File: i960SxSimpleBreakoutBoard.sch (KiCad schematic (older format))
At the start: 31 parts, among them J1 Conn_01x23, J2 Address LInes, J3 Data Lines, U1 80960Sx, U2 74HC573, U3 74HC573, U4 74HC245, U5 74HC245

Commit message: Fix a typo
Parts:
- J2: value Address LInes -> Address Lines
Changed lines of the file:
@@
 P 12450 5750
 F 0 "J2" H 12530 5742 50  0000 L CNN
-F 1 "Address LInes" H 12530 5651 50  0000 L CNN
+F 1 "Address Lines" H 12530 5651 50  0000 L CNN
 F 2 "" H 12450 5750 50  0001 C CNN
 F 3 "~" H 12450 5750 50  0001 C CNN

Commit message: Finish part selection
We shall see if the board gets too large from this change or not
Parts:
- J1: footprint (none) -> Connector_PinHeader_2.54mm:PinHeader_1x23_P2.54mm_Vertical
- J2: footprint (none) -> Connector_PinHeader_2.54mm:PinHeader_1x32_P2.54mm_Vertical
- J3: footprint (none) -> Connector_PinHeader_2.54mm:PinHeader_1x16_P2.54mm_Vertical
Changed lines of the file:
@@
 F 0 "J1" H 12530 2092 50  0000 L CNN
 F 1 "Conn_01x23" H 12530 2001 50  0000 L CNN
-F 2 "" H 12450 2050 50  0001 C CNN
+F 2 "Connector_PinHeader_2.54mm:PinHeader_1x23_P2.54mm_Vertical" H 12450 2050 50  0001 C CNN
 F 3 "~" H 12450 2050 50  0001 C CNN
 	1    12450 2050
@@
 F 0 "J2" H 12530 5742 50  0000 L CNN
 F 1 "Address Lines" H 12530 5651 50  0000 L CNN
-F 2 "" H 12450 5750 50  0001 C CNN
+F 2 "Connector_PinHeader_2.54mm:PinHeader_1x32_P2.54mm_Vertical" H 12450 5750 50  0001 C CNN
 F 3 "~" H 12450 5750 50  0001 C CNN
 	1    12450 5750
@@
 F 0 "J3" H 16630 5242 50  0000 L CNN
 F 1 "Data Lines" H 16630 5151 50  0000 L CNN
-F 2 "" H 16550 5250 50  0001 C CNN
+F 2 "Connector_PinHeader_2.54mm:PinHeader_1x16_P2.54mm_Vertical" H 16550 5250 50  0001 C CNN
 F 3 "~" H 16550 5250 50  0001 C CNN
 	1    16550 5250

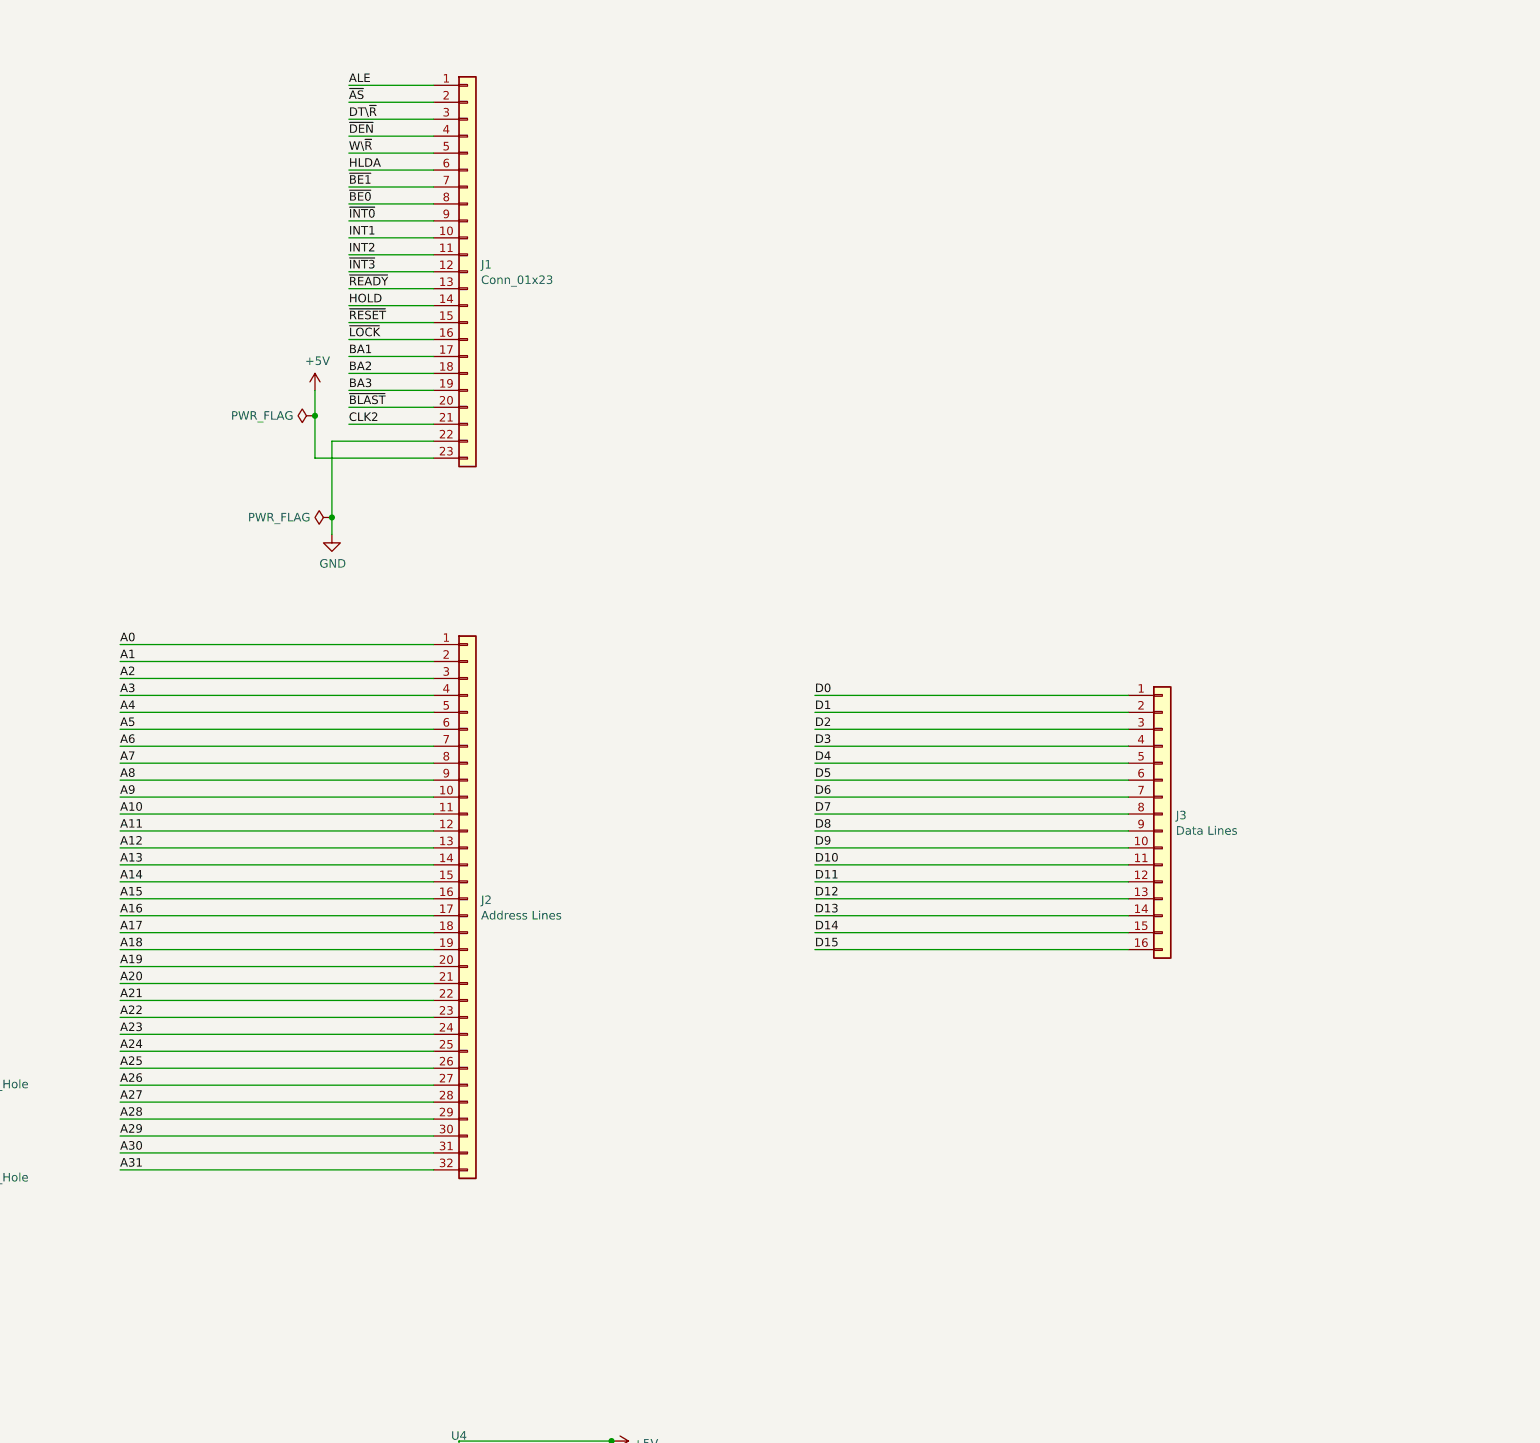
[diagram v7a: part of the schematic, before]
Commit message: Condense the pin headers further
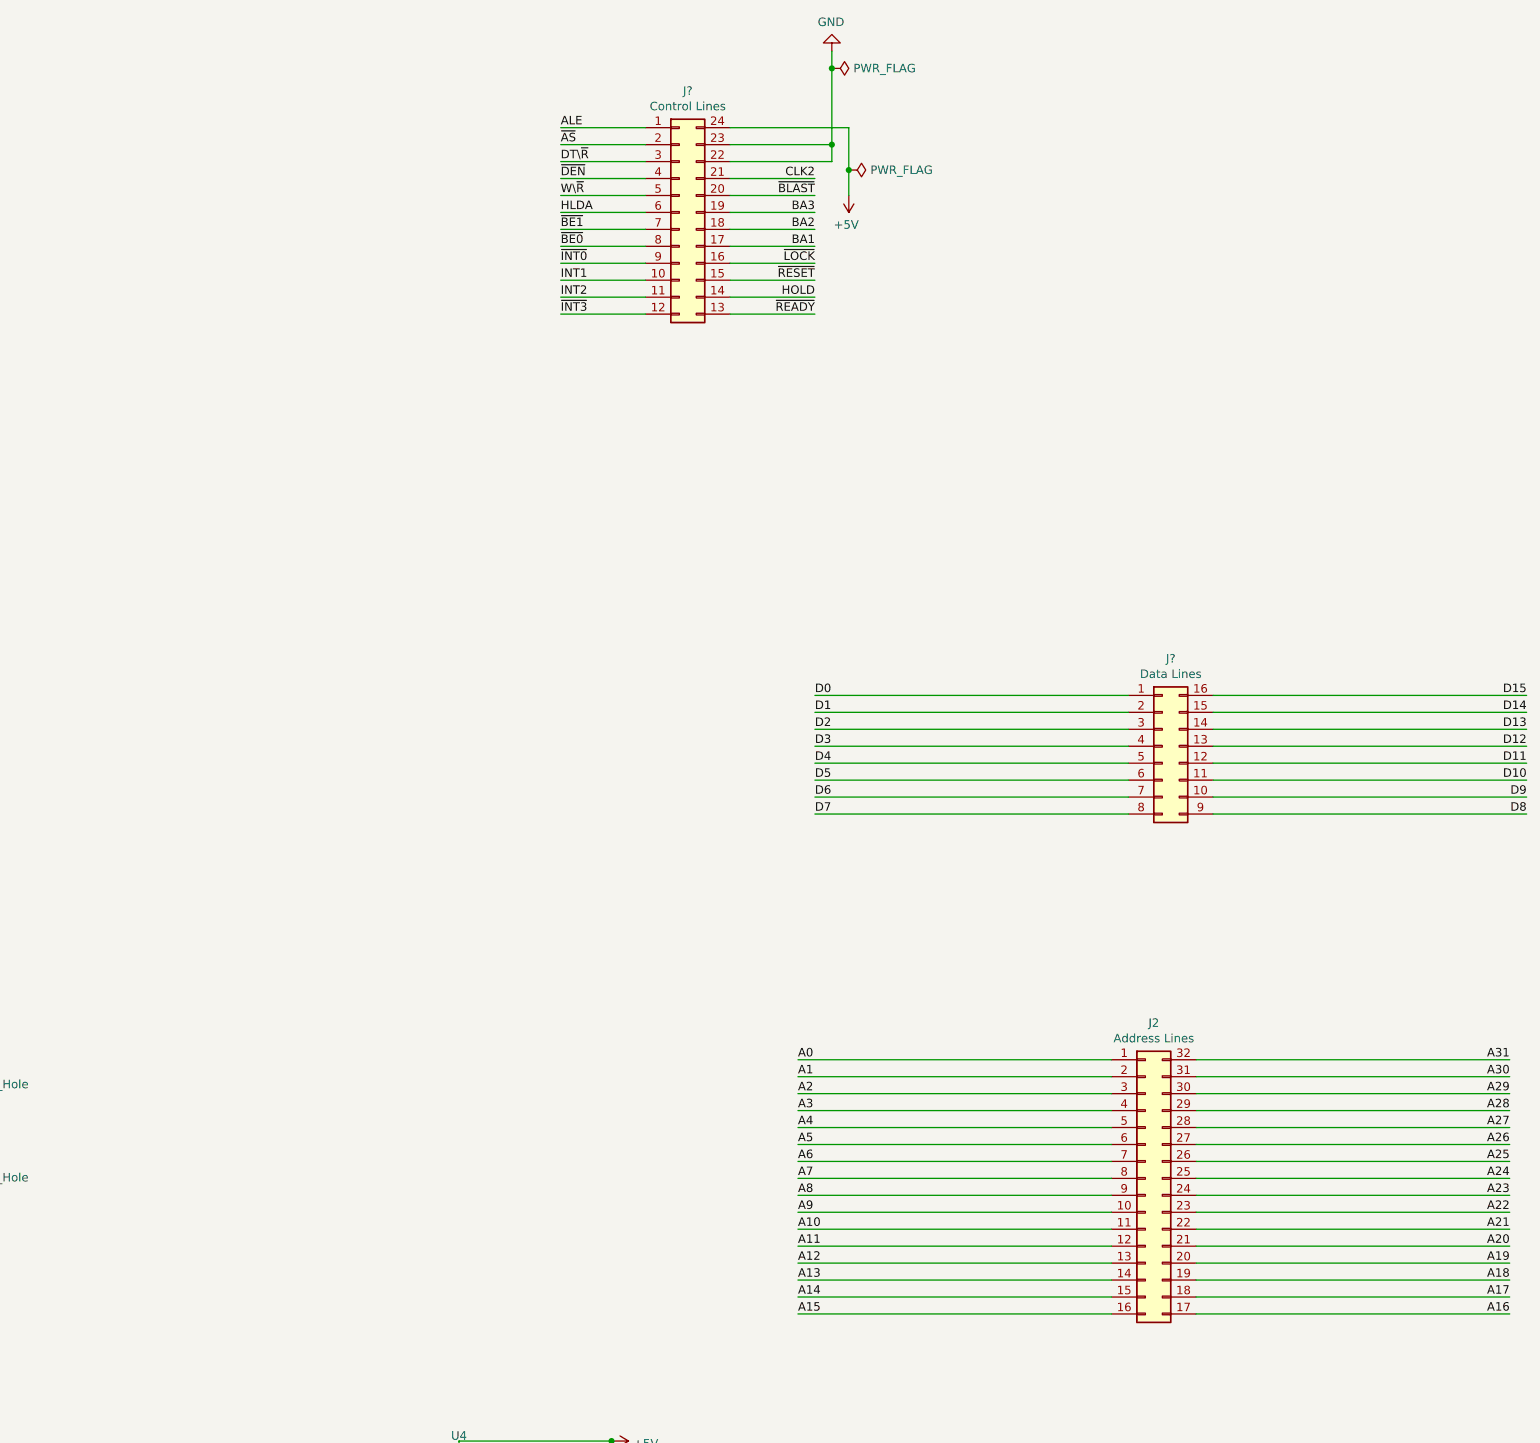
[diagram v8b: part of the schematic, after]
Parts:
- removed J1: Conn_01x23, Connector_PinHeader_2.54mm:PinHeader_1x23_P2.54mm_Vertical, symbol Connector_Generic:Conn_01x23
- removed J2: Address Lines, Connector_PinHeader_2.54mm:PinHeader_1x32_P2.54mm_Vertical, symbol Connector_Generic:Conn_01x32
- removed J3: Data Lines, Connector_PinHeader_2.54mm:PinHeader_1x16_P2.54mm_Vertical, symbol Connector_Generic:Conn_01x16
- added J2: Address Lines, Connector_PinHeader_2.54mm:PinHeader_2x16_P2.54mm_Vertical, symbol Connector_Generic:Conn_02x16_Counter_Clockwise
- added J?: Control Lines, symbol Connector_Generic:Conn_02x12_Counter_Clockwise
- added J?: Data Lines, symbol Connector_Generic:Conn_02x08_Counter_Clockwise
- U2, U3, U4, U5: footprint Package_DIP:DIP-20_W7.62mm_Socket -> Package_SO:SOIC-20W_7.5x12.8mm_P1.27mm
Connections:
- net +5V: now also J?.24 (Pin_24)
- net A0: now also J2.1 (Pin_1)
- net A1: now also J2.2 (Pin_2)
- net A10: now also J2.11 (Pin_11)
- net A11: now also J2.12 (Pin_12)
- net A12: now also J2.13 (Pin_13)
- net A13: now also J2.14 (Pin_14)
- net A14: now also J2.15 (Pin_15)
- net A15: now also J2.16 (Pin_16)
- net A16: now also J2.17 (Pin_17)
- net A17: now also J2.18 (Pin_18)
- net A18: now also J2.19 (Pin_19)
- net A19: now also J2.20 (Pin_20)
- net A2: now also J2.3 (Pin_3)
- net A20: now also J2.21 (Pin_21)
- net A21: now also J2.22 (Pin_22)
- net A22: now also J2.23 (Pin_23)
- net A23: now also J2.24 (Pin_24)
- net A24: now also J2.25 (Pin_25)
- net A25: now also J2.26 (Pin_26)
- net A26: now also J2.27 (Pin_27)
- net A27: now also J2.28 (Pin_28)
- net A28: now also J2.29 (Pin_29)
- net A29: now also J2.30 (Pin_30)
- net A3: now also J2.4 (Pin_4)
- net A30: now also J2.31 (Pin_31)
- net A31: now also J2.32 (Pin_32)
- net A4: now also J2.5 (Pin_5)
- net A5: now also J2.6 (Pin_6)
- net A6: now also J2.7 (Pin_7)
- net A7: now also J2.8 (Pin_8)
- net A8: now also J2.9 (Pin_9)
- net A9: now also J2.10 (Pin_10)
- net ALE: now also J?.1 (Pin_1)
- net BA1: now also J?.17 (Pin_17)
- net BA2: now also J?.18 (Pin_18)
- net BA3: now also J?.19 (Pin_19)
- net CLK2: now also J?.21 (Pin_21)
- net D0: now also J?.1 (Pin_1)
- net D1: now also J?.2 (Pin_2)
- net D10: now also J?.11 (Pin_11)
- net D11: now also J?.12 (Pin_12)
- net D12: now also J?.13 (Pin_13)
- net D13: now also J?.14 (Pin_14)
- net D14: now also J?.15 (Pin_15)
- net D15: now also J?.16 (Pin_16)
- net D2: now also J?.3 (Pin_3)
- net D3: now also J?.4 (Pin_4)
- net D4: now also J?.5 (Pin_5)
- net D5: now also J?.6 (Pin_6)
- net D6: now also J?.7 (Pin_7)
- net D7: now also J?.8 (Pin_8)
- net D8: now also J?.9 (Pin_9)
- net D9: now also J?.10 (Pin_10)
- net DT\~R: now also J?.3 (Pin_3)
- net GND: now also J?.22 (Pin_22), J?.23 (Pin_23)
- net HLDA: now also J?.6 (Pin_6)
- net HOLD: now also J?.14 (Pin_14)
- net INT1: now also J?.10 (Pin_10)
- net INT2: now also J?.11 (Pin_11)
- net W\~R: now also J?.5 (Pin_5)
- net ~AS: now also J?.2 (Pin_2)
- net ~BE0: now also J?.8 (Pin_8)
- net ~BE1: now also J?.7 (Pin_7)
- net ~BLAST: now also J?.20 (Pin_20)
- net ~DEN: now also J?.4 (Pin_4)
- net ~INT0: now also J?.9 (Pin_9)
- net ~INT3: now also J?.12 (Pin_12)
- net ~LOCK: now also J?.16 (Pin_16)
- net ~READY: now also J?.13 (Pin_13)
- net ~RESET: now also J?.15 (Pin_15)
